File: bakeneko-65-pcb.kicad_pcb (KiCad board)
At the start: 2 copper layers, 299.8 x 100.1 mm, 166 parts, among them J1 JST SH 4-pin, J2 AVR-ISP-6, J3 Conn_01x06_Female, SW1 Reset, U1 SRV05-4, U2 ATmega32U4-AU, Y1 16MHz

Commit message: remove usb
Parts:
- removed USB2: HRO-TYPE-C-31-M-12, Type-C:HRO-TYPE-C-31-M-12
- J3: value Conn_01x06_Female -> Conn_01x04_Female; footprint Connector_PinHeader_1.00mm:PinHeader_1x06_P1.00mm_Vertical -> Connector_PinHeader_1.00mm:PinHeader_1x04_P1.00mm_Vertical
- moved R6 19.8 mm to (161.0, 1.91), turned to 180 degrees
- moved R5 19.1 mm to (141.1, 1.91), turned to 0 degrees
- moved J3 9.08 mm to (153.8, 13.0)
- moved USB1 2.48 mm to (152.3, -4.50)
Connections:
- J3 pad 2: CC1 -> D+
- J3 pad 3: D+ -> D-
- J3 pad 4: D- -> VBUS
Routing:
- net GND: track 346.5 -> 324.2 mm, vias 8 -> 5
- net CC2: track 25.3 -> 8.47 mm, vias 2 -> 0
- net CC1: track 25.1 -> 11.1 mm, vias 2 -> 0
- net VBUS: track 156.5 -> 147.5 mm, vias 1 -> 2
- net D-: track 143.5 -> 134.9 mm, vias 1 -> 0
- net D+: track 143.9 -> 137.3 mm, vias 2 -> 0
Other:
- board size 299.8 x 100.1 mm -> 299.8 x 97 mm
- board text removed: "Bakeneko65 v3.0"

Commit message: add USB c
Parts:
- added USB2: HRO-TYPE-C-31-M-12, Type-C:HRO-TYPE-C-31-M-12, B.Cu at (152.3, -6.25)
- moved USB1 1.09 mm to (152.3, -3.41)
- turned R5 to 180 degrees
- turned R6 to 0 degrees
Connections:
- net CC1 renamed Net-(USB1-CC1)
- net CC2 renamed Net-(USB1-CC2)
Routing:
- net VBUS: track 147.5 -> 161.1 mm, vias 2 -> 3
- net GND: track 324.2 -> 335.4 mm
- net Net-(USB1-CC1): track 11.1 -> 20.4 mm, vias 0 -> 2
- net Net-(USB1-CC2): track 8.47 -> 17.5 mm, vias 0 -> 2
- net D+: track 137.3 -> 142.1 mm
- net D-: track 134.9 -> 139.6 mm
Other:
- board size 299.8 x 97 mm -> 299.8 x 98.7 mm

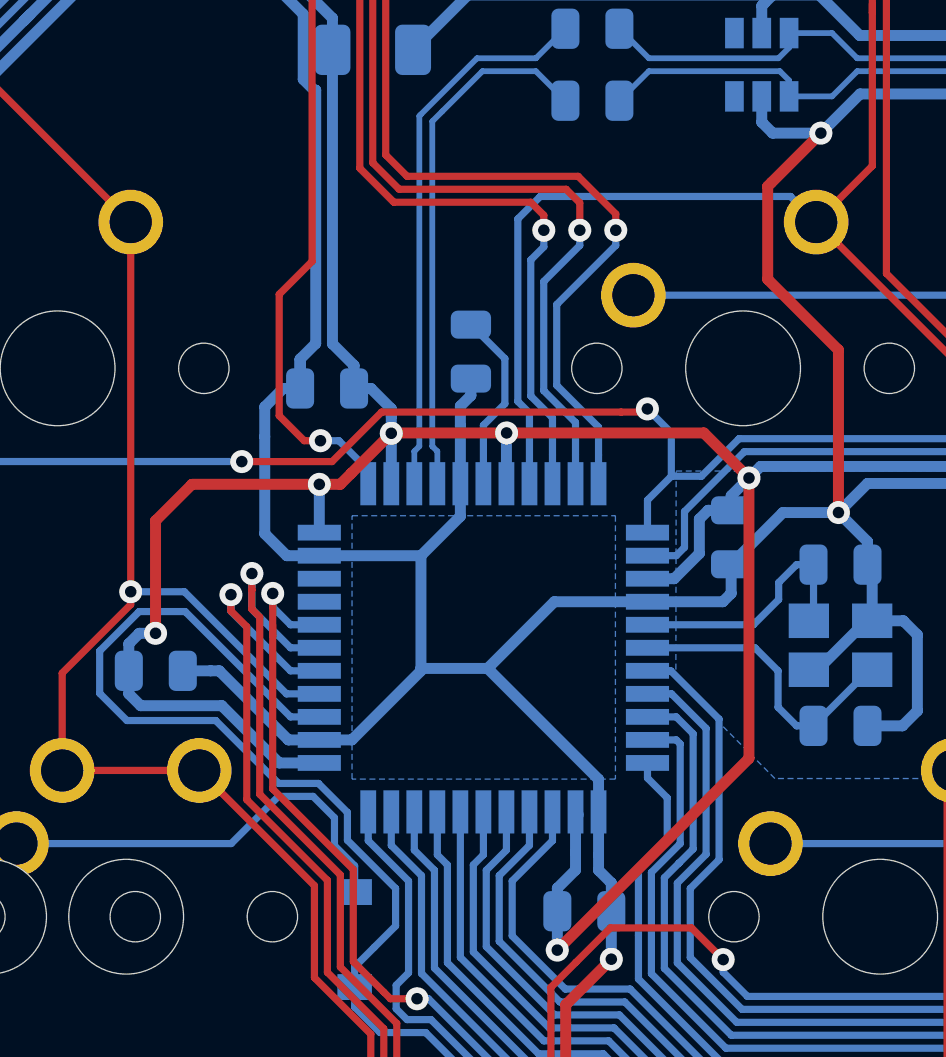
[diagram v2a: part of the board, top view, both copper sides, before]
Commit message: change Atmega AU to MU
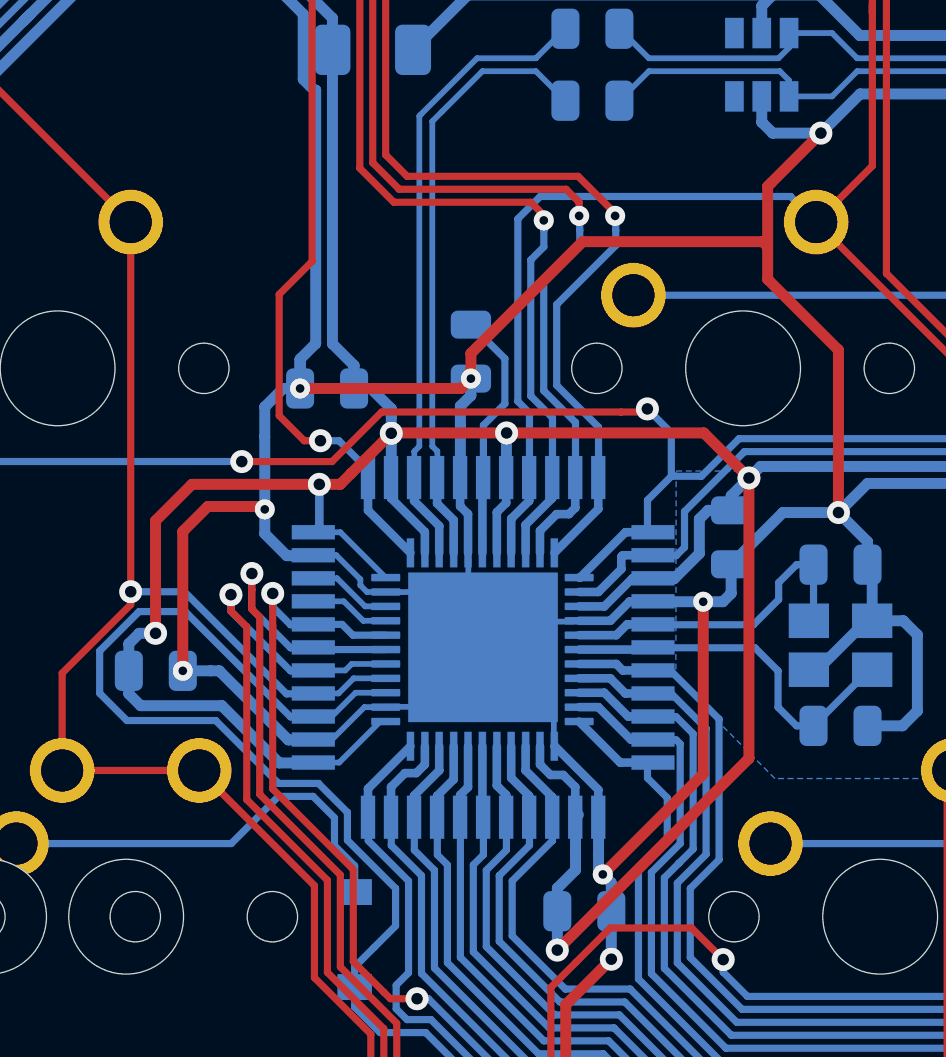
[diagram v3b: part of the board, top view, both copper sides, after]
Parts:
- U2: footprint Package_QFP:TQFP-44_10x10mm_P0.8mm -> tahutech:Hybrid Atmega32u4
- moved U2 1.06 mm to (27.9, 38.0)
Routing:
- net GND: track 335.4 -> 358.3 mm, vias 5 -> 11
- net +5V: track 123.2 -> 141.6 mm
- net MOSI: track 44.8 -> 48.2 mm
- net RESET: track 88.5 -> 91.8 mm
- net MISO: track 55.0 -> 58.3 mm
- net ROW0: track 296.2 -> 299.4 mm
- net ROW1: track 284.9 -> 288.1 mm
- net COL3: track 125.1 -> 128.3 mm
- net COL11: track 293.6 -> 296.8 mm
- net Net-(U2-~{HWB}/PE2): track 14.6 -> 17.7 mm
- net COL12: track 318.3 -> 321.3 mm
- net SCK: track 45.7 -> 48.7 mm
- net /MCU_D-: track 19.2 -> 22.2 mm
- net unconnected-(U2-AREF-Pad42): track 0.00 -> 2.92 mm
- net COL13: track 353.1 -> 356.0 mm
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
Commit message: rev
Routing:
- net COL15: track 357.7 -> 360.3 mm
- net COL14: track 321.7 -> 323.4 mm
- net COL13: track 356.0 -> 357.5 mm
- net COL12: track 321.3 -> 322.7 mm

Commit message: update
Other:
- board text added: "65U 0.1"
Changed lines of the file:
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@@
   )
   (setup
+    (stackup
+      (layer "F.SilkS" (type "Top Silk Screen"))
+      (layer "F.Paste" (type "Top Solder Paste"))
+      (layer "F.Mask" (type "Top Solder Mask") (thickness 0.01))
+      (layer "F.Cu" (type "copper") (thickness 0.035))
+      (layer "dielectric 1" (type "core") (thickness 1.51) (material "FR4") (epsilon_r 4.5) (loss_tangent 0.02))
+      (layer "B.Cu" (type "copper") (thickness 0.035))
+      (layer "B.Mask" (type "Bottom Solder Mask") (thickness 0.01))
+      (layer "B.Paste" (type "Bottom Solder Paste"))
+      (layer "B.SilkS" (type "Bottom Silk Screen"))
+      (copper_finish "None")
+      (dielectric_constraints no)
+    )
     (pad_to_mask_clearance 0.05)
     (grid_origin 4.60375 43.18)
@@
       (plot_on_all_layers_selection 0x0000000_00000000)
       (disableapertmacros false)
-      (usegerberextensions false)
+      (usegerberextensions true)
       (usegerberattributes false)
       (usegerberadvancedattributes false)
@@
       (plotinvisibletext false)
       (sketchpadsonfab false)
-      (subtractmaskfromsilk false)
+      (subtractmaskfromsilk true)
       (outputformat 1)
       (mirror false)
       (drillshape 0)
       (scaleselection 1)
-      (outputdirectory "./gerber")
+      (outputdirectory "Gerber/Zed65/")
     )
   )
@@
   (gr_line (start 2.39375 4.24) (end 2.39375 0.15)
     (stroke (width 0.1) (type default)) (layer "Margin"))
+  (gr_text "65U 0.1" (at 157.00375 86.0425) (layer "F.SilkS")
+    (effects (font (size 2.5 2.5) (thickness 0.3)) (justify left bottom))
+  )
   (segment (start 38.8225 24.975) (end 38.8225 23.84) (width 0.381) (layer "F.Cu") (net 1))
   (segment (start 36.58375 42.16348) (end 36.58375 36.17875) (width 0.381) (layer "F.Cu") (net 1))
